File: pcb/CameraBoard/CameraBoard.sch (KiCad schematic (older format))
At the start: 17 parts, among them P2 CONN_01X03, P3 CONN_01X03, P4 CONN_01X08, U1 arduino_mini, U2 notgate_74HCT04

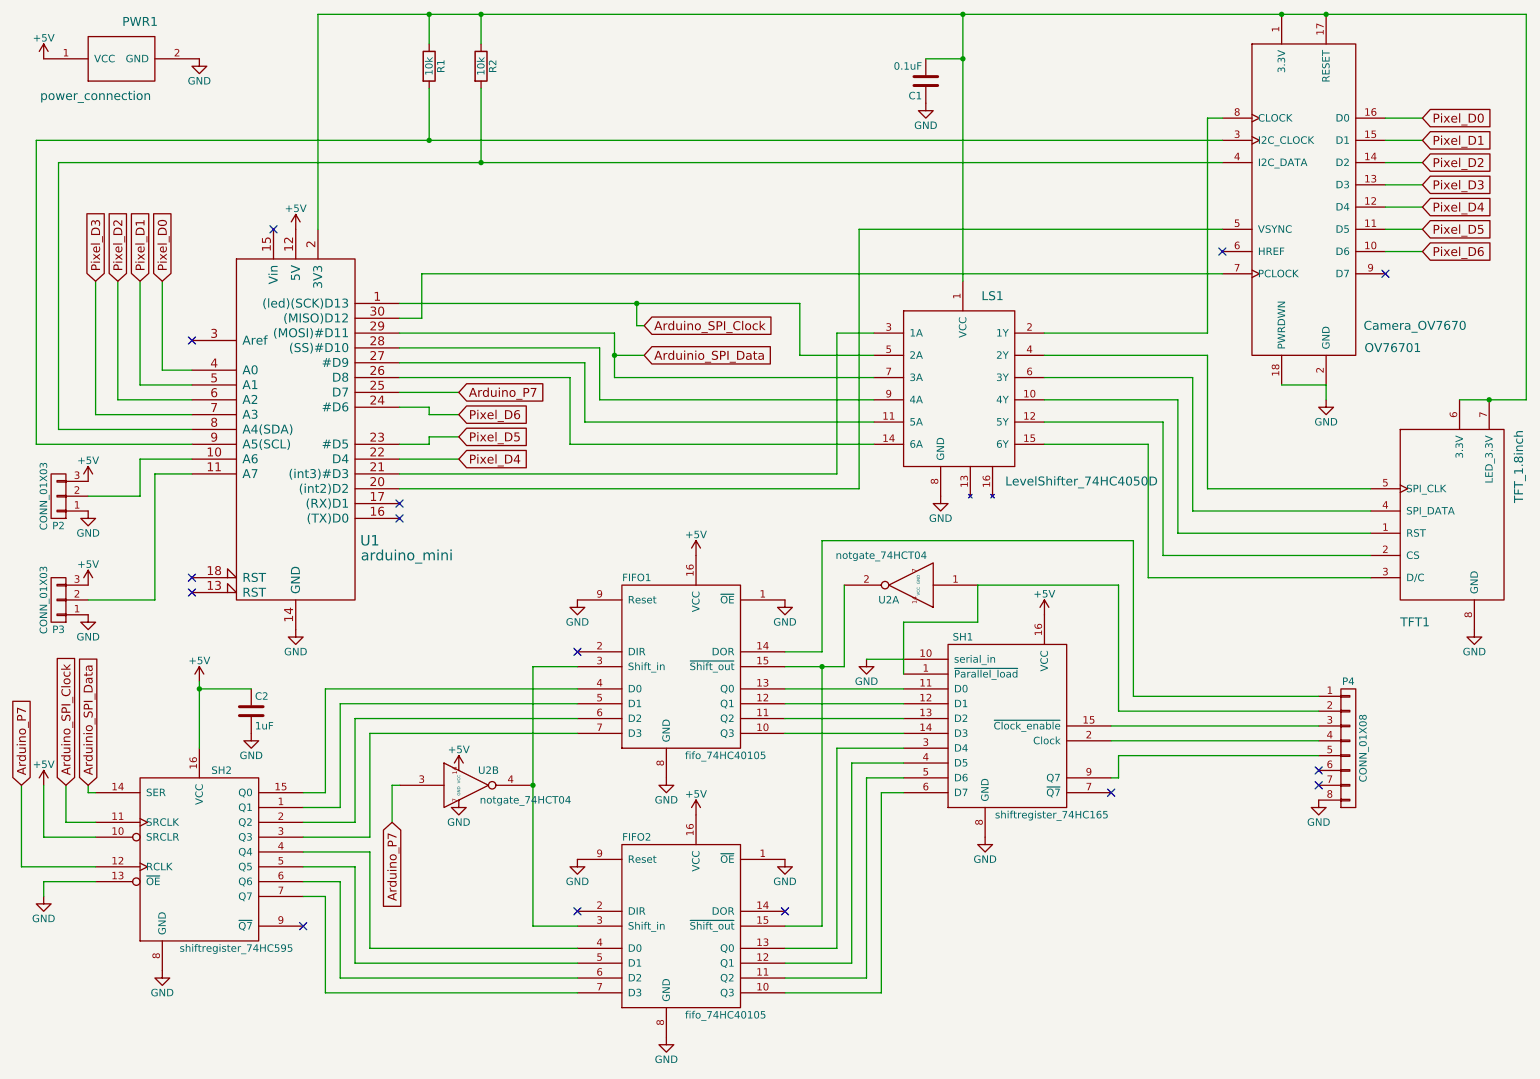
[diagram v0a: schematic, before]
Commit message: send data to shift register
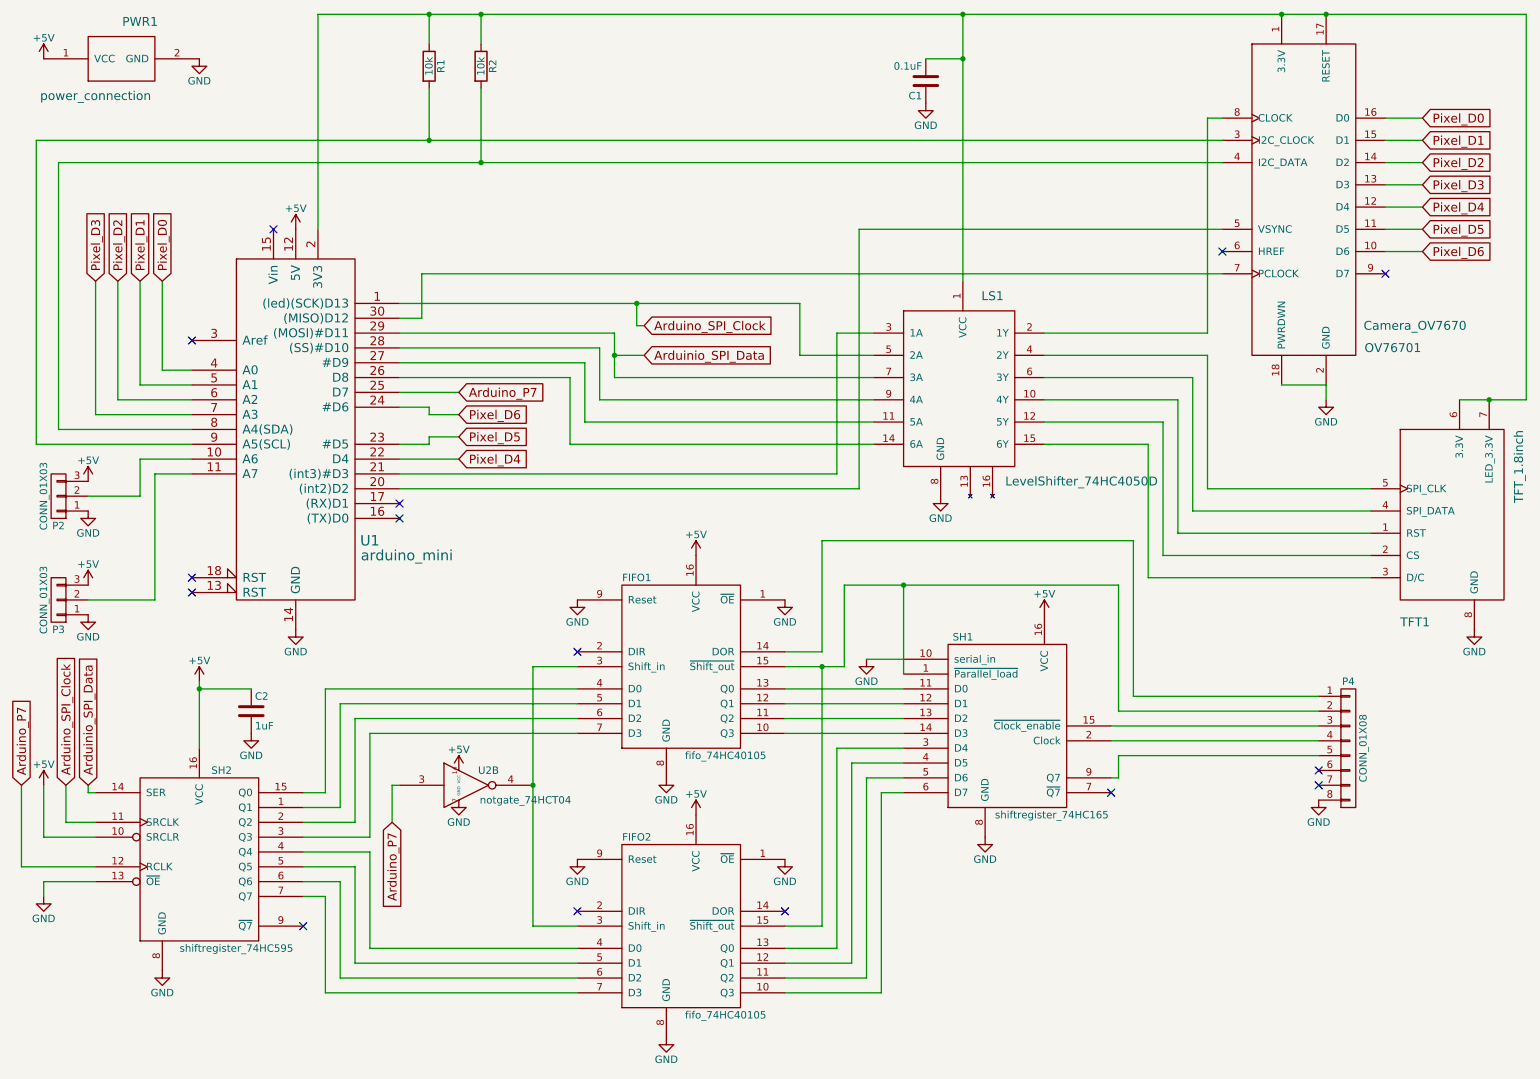
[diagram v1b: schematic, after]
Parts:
- removed unit 1 of U2
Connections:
- net at P4.2 (P2), SH1.1 (~Parallel_load): now also FIFO1.15 (~Shift_out), FIFO2.15 (~Shift_out)
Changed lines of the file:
@@
 	6450 2950 5950 2950
 Wire Wire Line
-	5950 2950 5950 2600
+	5950 2600 5950 2950
 Wire Wire Line
 	3400 2400 8800 2400
@@
 	1200 3350 1200 2450
 Wire Wire Line
-	10850 3250 10850 650
+	10850 650  10850 3250
 Wire Wire Line
 	2700 650  2700 2100
 Wire Wire Line
-	10850 650  2700 650
+	2700 650  10850 650
 Connection ~ 9200 650
 Connection ~ 9500 650
@@
 	6200 5600 6650 5600
 Wire Wire Line
-	5950 2600 3250 2600
+	3250 2600 5950 2600
 Wire Wire Line
 	4900 2950 4700 2950
@@
 Wire Wire Line
 	6100 4200 8200 4200
-$Comp
-L notgate_74HCT04 U2
-U 1 1 5738EBCE
-P 6700 4500
-F 0 "U2" H 6850 4600 50  0000 C CNN
-F 1 "notgate_74HCT04" H 6900 4300 50  0000 C CNN
-F 2 "Housings_SOIC:SOIC-14_3.9x8.7mm_Pitch1.27mm" H 6700 4500 50  0001 C CNN
-F 3 "" H 6700 4500 50  0000 C CNN
-	1    6700 4500
-	-1   0    0    1
-$EndComp
 Wire Wire Line
 	6250 5050 6250 4500
@@
 	5850 5050 6250 5050
 Wire Wire Line
-	7150 4500 7150 4750
-Wire Wire Line
-	7150 4750 6650 4750
-Wire Wire Line
-	6650 4750 6650 5100
-Wire Wire Line
-	7150 4500 8100 4500
+	6650 4500 6650 5100
+Wire Wire Line
+	6250 4500 8100 4500
 Wire Wire Line
 	8050 5450 9450 5450
@@
 	1    0    0    -1
 $EndComp
+Connection ~ 6650 4500
 $EndSCHEMATC
